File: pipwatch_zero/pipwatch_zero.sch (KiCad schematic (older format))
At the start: 0 parts

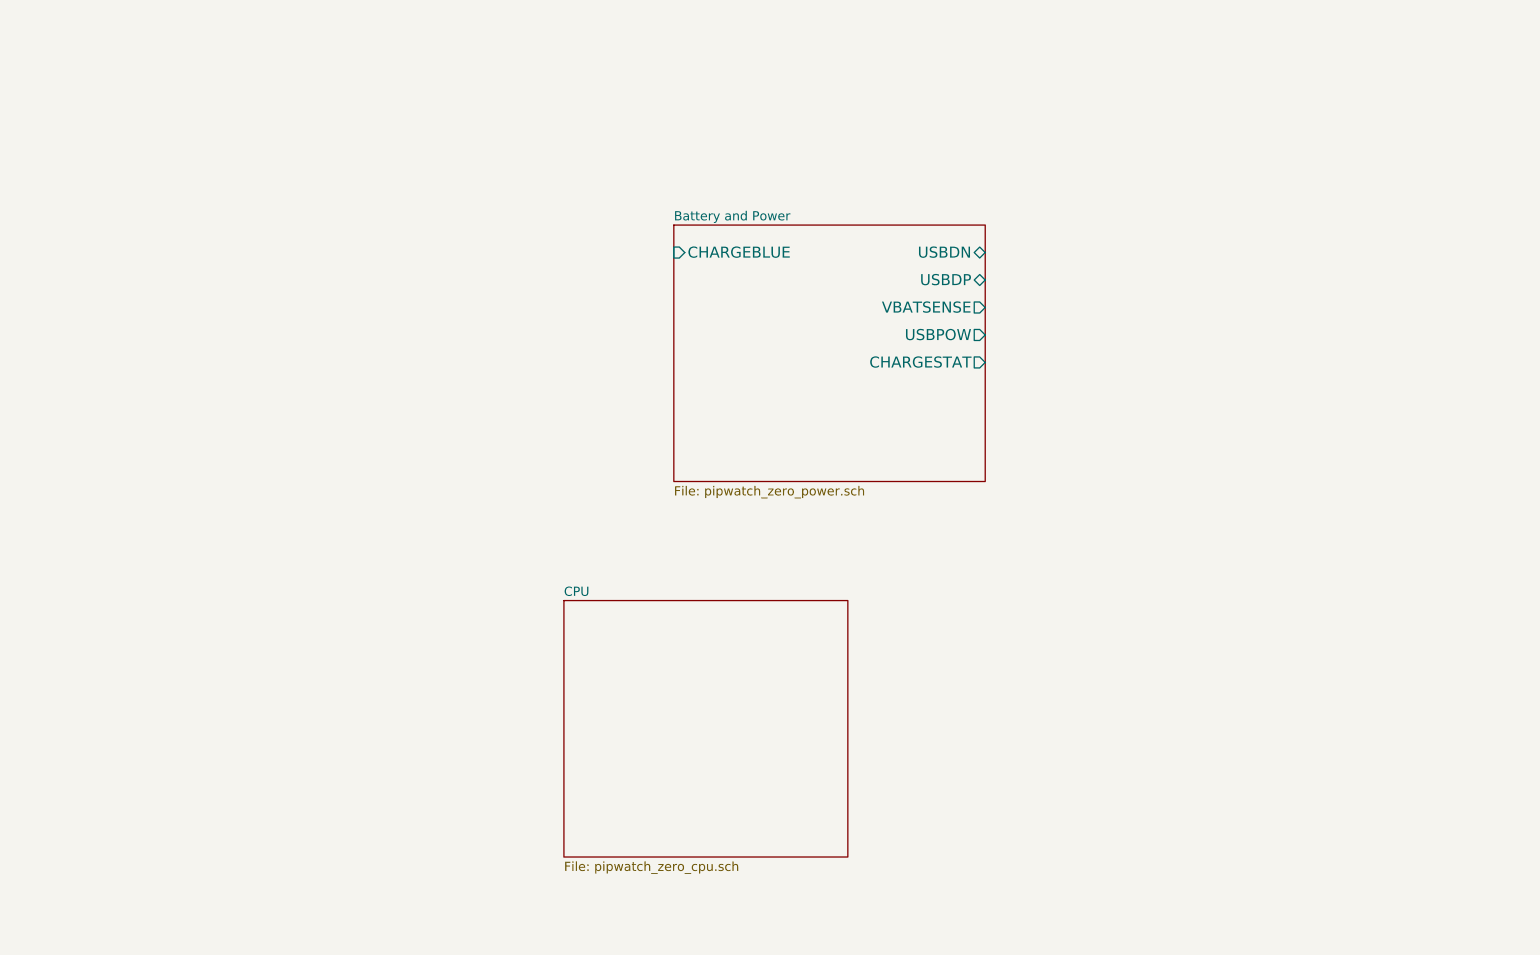
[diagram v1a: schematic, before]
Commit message: pipwatch_zero: basic schema complete
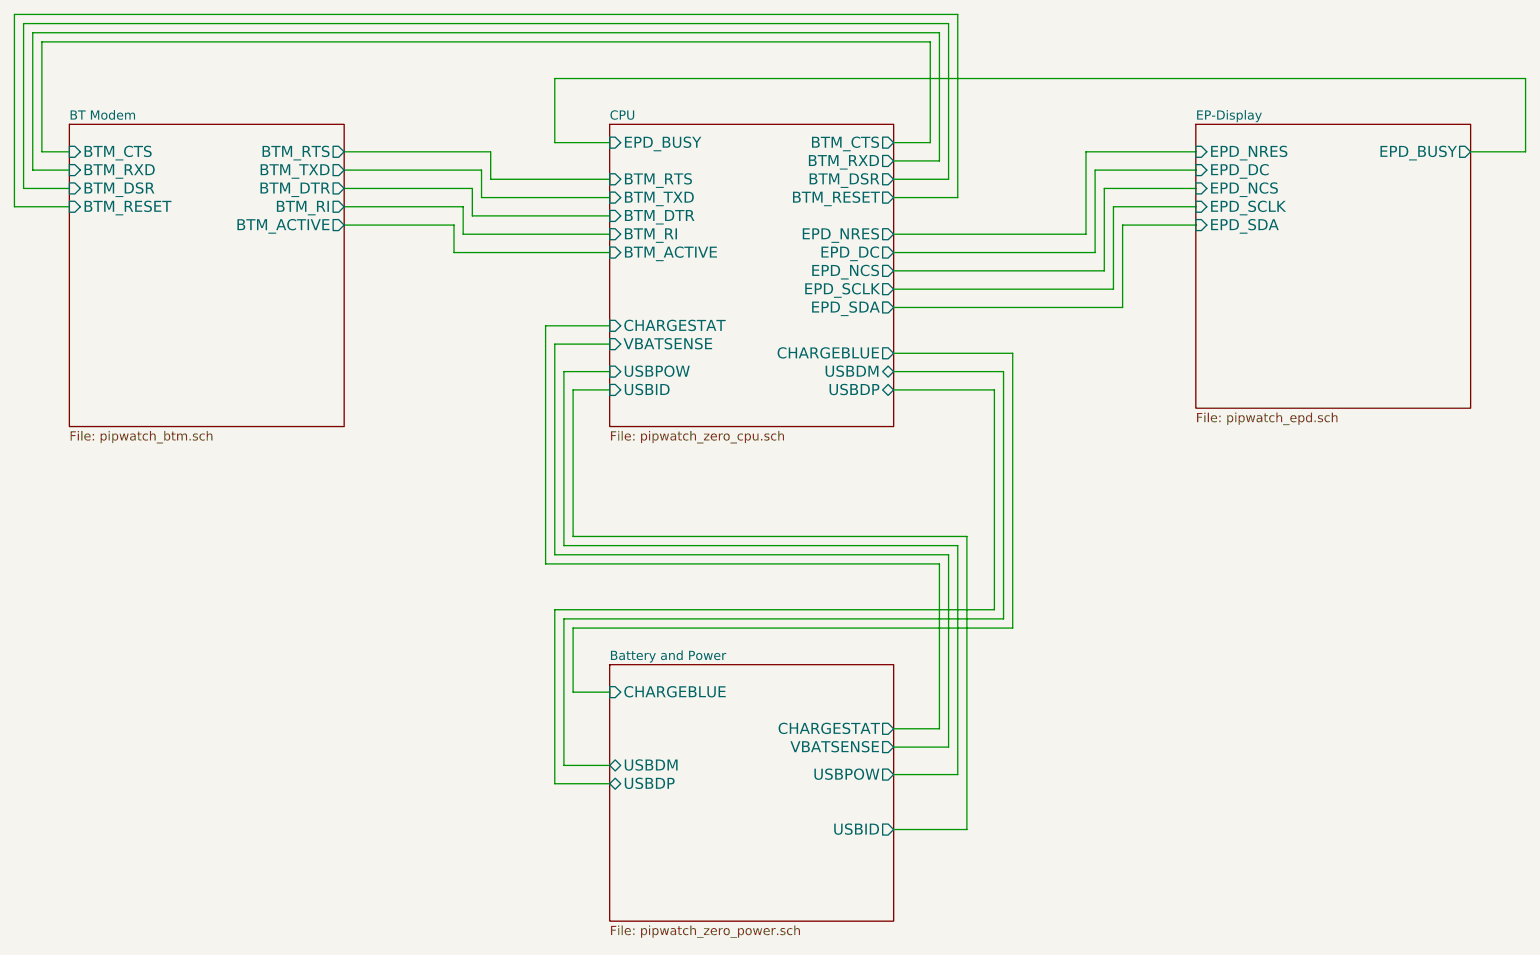
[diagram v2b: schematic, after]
